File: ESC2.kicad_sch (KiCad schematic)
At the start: 35 parts, among them J10 MOTOR1, J9 SWD1, Q5 XRS306D, Q6 XRS306D, Q7 XRS306D, U10 DRV8300D, U9 STM32G071GBUxN

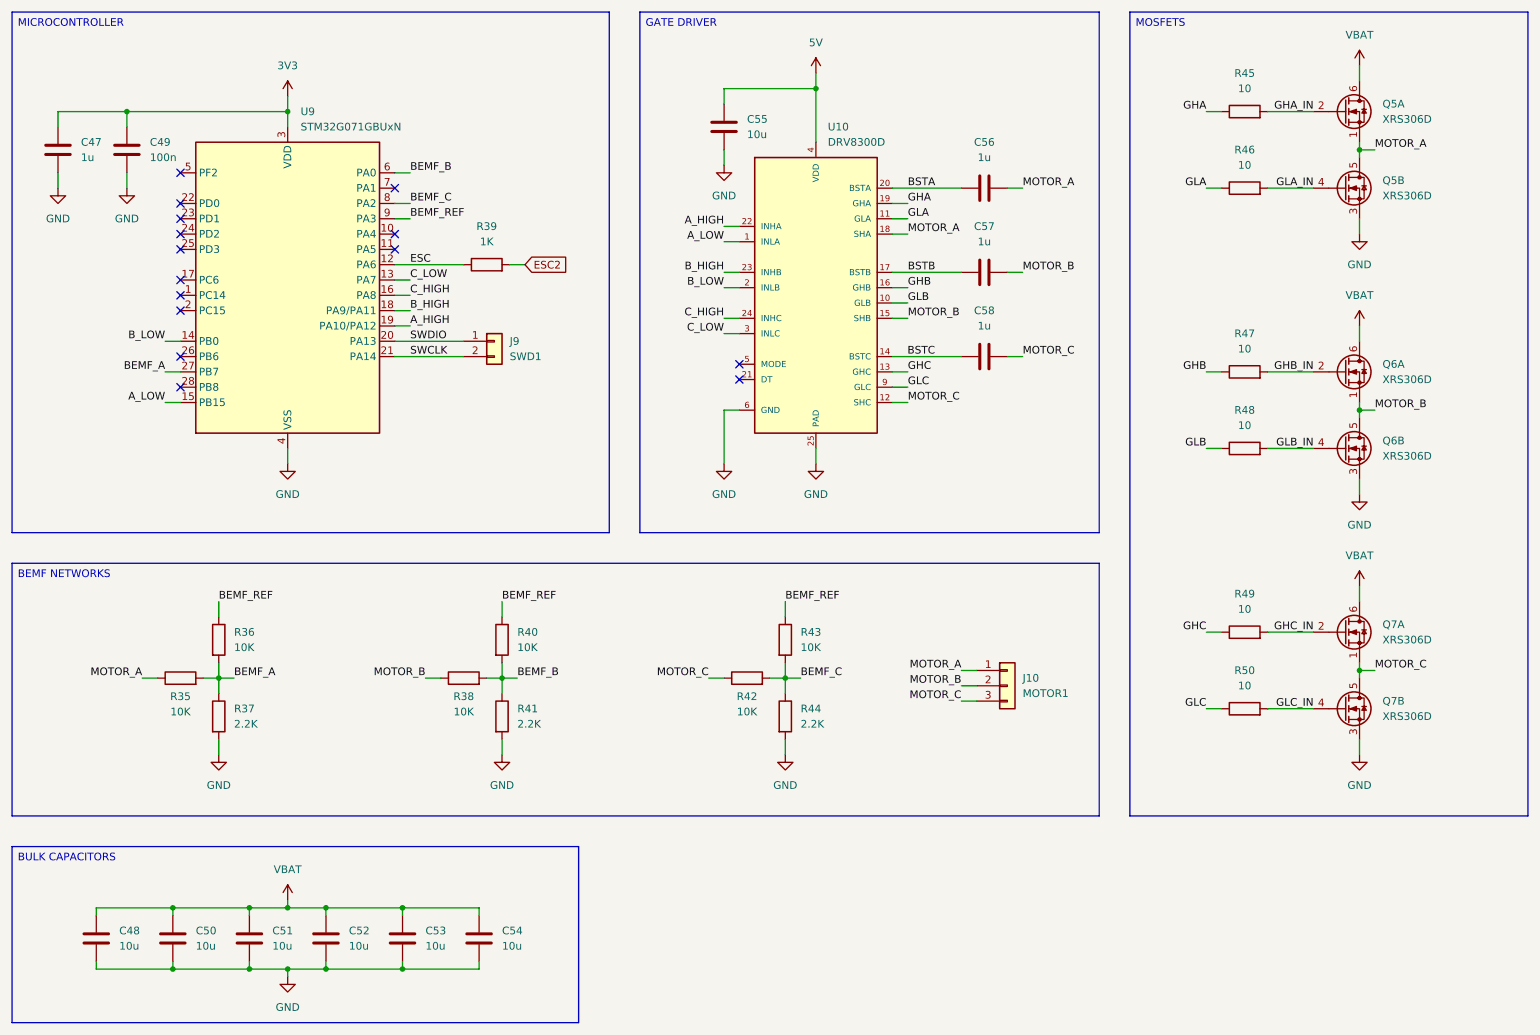
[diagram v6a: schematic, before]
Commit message: Initial layout
Completed an initial layout of the main components.

TODO
Route the ESCs and check the result.
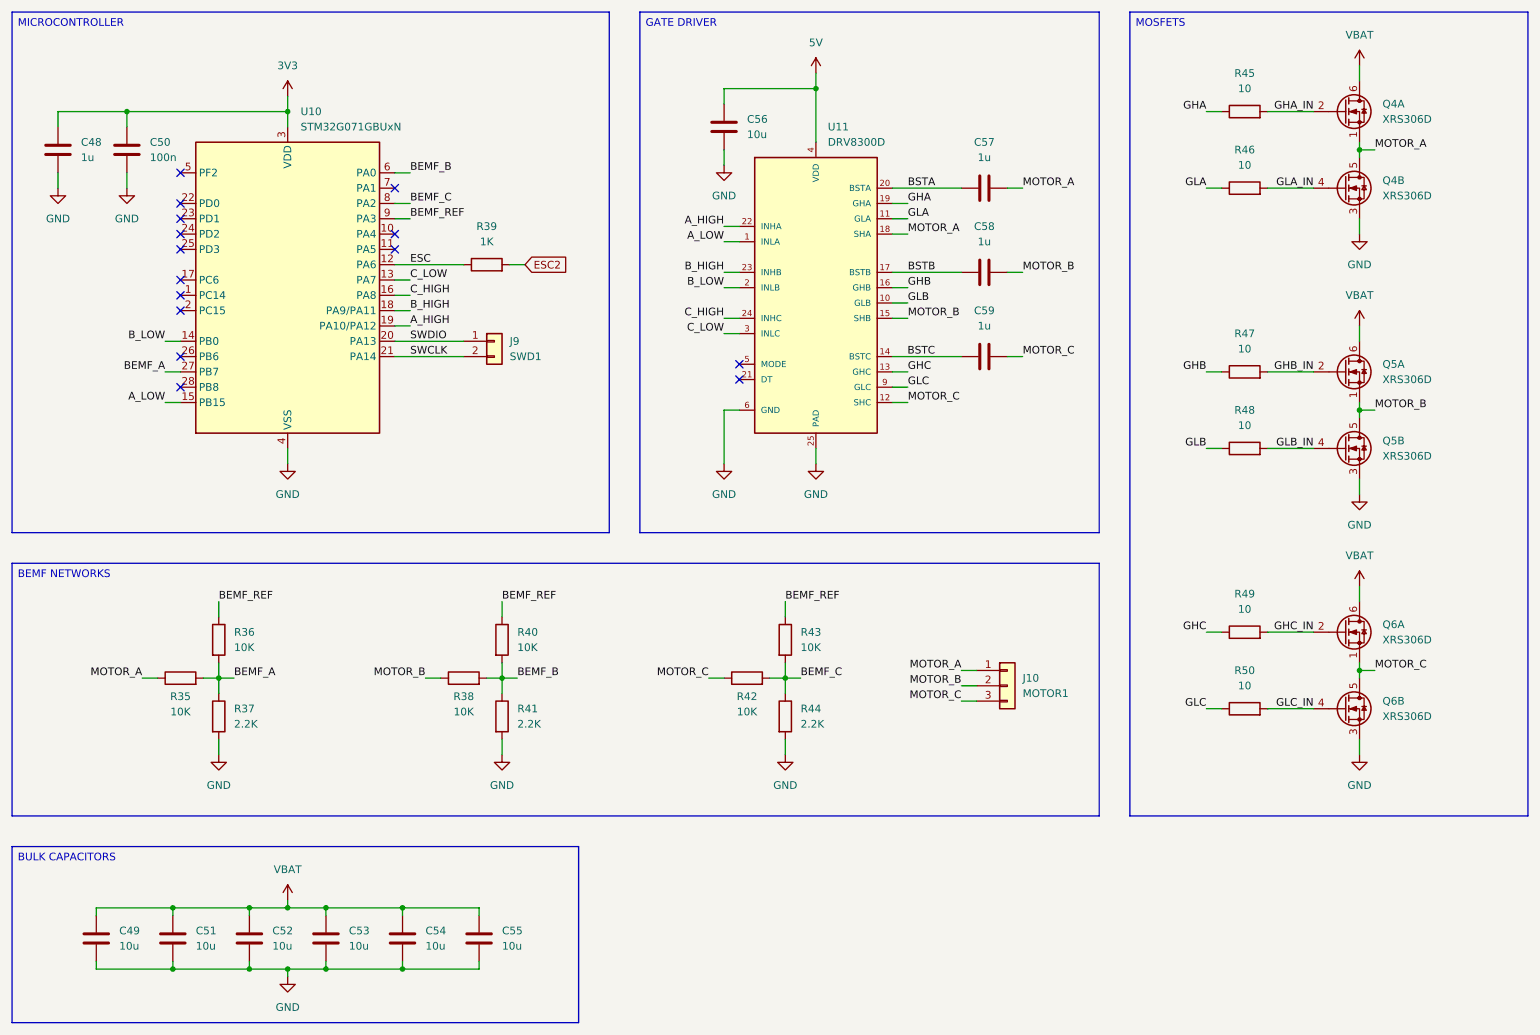
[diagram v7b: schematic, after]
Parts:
- renumbered C47 to C48, C48 to C49, C49 to C50, C50 to C51, C51 to C52, C52 to C53, C53 to C54, C54 to C55, C55 to C56, C56 to C57, C57 to C58, C58 to C59, Q5 to Q4, Q6 to Q5, Q7 to Q6, U9 to U10, U10 to U11

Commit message: Settings and ESC layout
Updated the PCB configuration options for manufacturing.
Completed the initial ESC layout.

TODO:
Replicate ESC layout.
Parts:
- J10: footprint Custom_Parts:PAD_3_SQUARE_SOLID_2.5x2.5mm_P4.0mm -> Custom_Parts:PAD_3_SQUARE_SOLID_2.5x2.5mm_P4.0mm_MOTOR
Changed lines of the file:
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@@
 			)
 		)
-		(property "Footprint" "Custom_Parts:PAD_3_SQUARE_SOLID_2.5x2.5mm_P4.0mm"
+		(property "Footprint" "Custom_Parts:PAD_3_SQUARE_SOLID_2.5x2.5mm_P4.0mm_MOTOR"
 			(at 187.96 134.62 0)
 			(effects
